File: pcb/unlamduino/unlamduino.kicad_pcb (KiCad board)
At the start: 2 copper layers, 106.7 x 69.8 mm, 41 parts, among them IC2 ATMEGA328-P, P3 CONN_01X08, U1 LM2576, U2 AP111733, Y2 16MHz

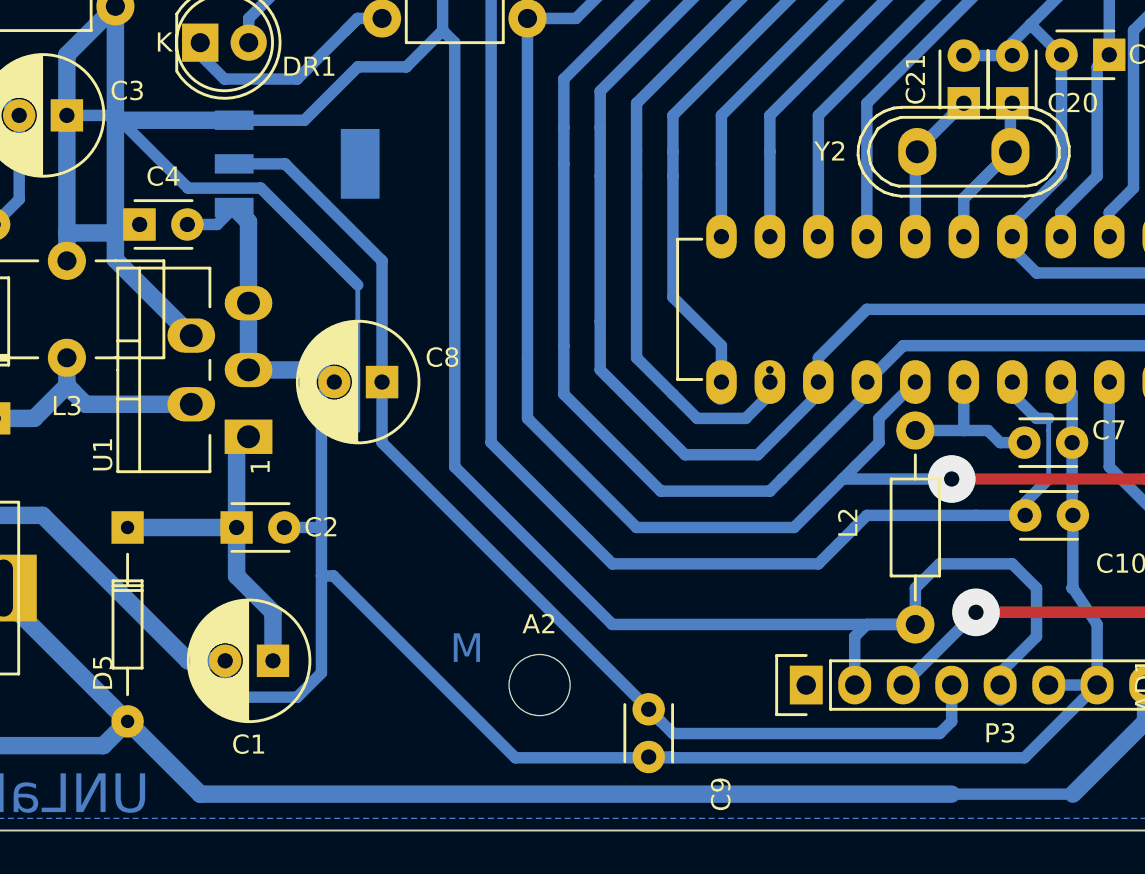
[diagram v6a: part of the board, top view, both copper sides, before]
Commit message: cambio de 5v en conector para no pasar por el medio de un capa.
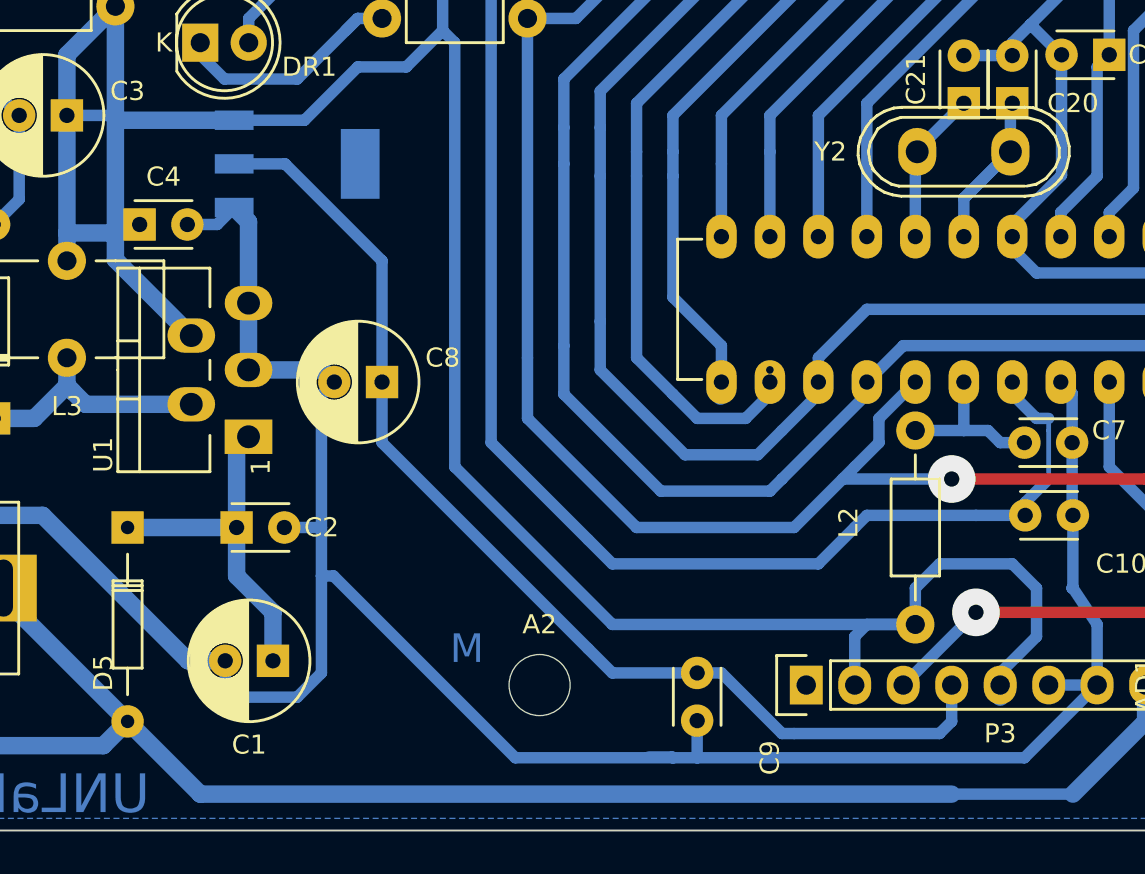
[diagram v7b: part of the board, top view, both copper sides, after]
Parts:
- moved C9 3.17 mm to (199.4, 100.3)
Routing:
- net +5V: track 341.6 -> 317.9 mm
- net GND: track 449.4 -> 451.3 mm
- net +3V3: track 59.2 -> 58.3 mm
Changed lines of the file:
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@@
     (thickness 1.6)
     (drawings 16)
-    (tracks 542)
+    (tracks 543)
     (zones 0)
     (modules 41)
@@
   )
   (module Capacitors_ThroughHole:C_Disc_D3_P2.5 (layer F.Cu)
-    (at 196.85 102.235 270)
+    (at 199.39 100.33 270)
     (descr "Capacitor 3mm Disc, Pitch 2.5mm")
     (tags Capacitor)
@@
   (segment (start 199.39 49.53) (end 226.695 49.53) (width 0.6) (layer B.Cu) (net 6))
   (segment (start 198.501 52.705) (end 198.501 51.689) (width 0.9144) (layer B.Cu) (net 6) (status 30))
-  (segment (start 196.85 104.735) (end 198.08 104.735) (width 0.6) (layer B.Cu) (net 7) (status 400000))
+  (segment (start 199.39 104.775) (end 199.39 102.83) (width 0.6) (layer B.Cu) (net 7) (status 800000))
+  (segment (start 196.85 104.735) (end 198.08 104.735) (width 0.6) (layer B.Cu) (net 7))
   (segment (start 198.08 104.735) (end 198.12 104.775) (width 0.6) (layer B.Cu) (net 7))
   (segment (start 180.3 59.055) (end 180.34 59.055) (width 0.6) (layer B.Cu) (net 7))
@@
   (segment (start 177.8 64.135) (end 179.07 62.865) (width 0.6) (layer B.Cu) (net 7))
   (segment (start 189.865 104.775) (end 198.12 104.775) (width 0.6) (layer B.Cu) (net 7))
-  (segment (start 198.12 104.775) (end 216.535 104.775) (width 0.6) (layer B.Cu) (net 7))
+  (segment (start 198.12 104.775) (end 199.39 104.775) (width 0.6) (layer B.Cu) (net 7))
+  (segment (start 199.39 104.775) (end 216.535 104.775) (width 0.6) (layer B.Cu) (net 7))
   (segment (start 189.865 104.775) (end 180.34 95.25) (width 0.6) (layer B.Cu) (net 7))
   (segment (start 179.705 95.25) (end 180.34 95.25) (width 0.6) (layer B.Cu) (net 7))
@@
   (segment (start 175.26 88.57996) (end 175.88484 87.95512) (width 0.6) (layer B.Cu) (net 8) (status 30))
   (segment (start 169.54754 92.71052) (end 174.93944 92.71052) (width 0.9144) (layer B.Cu) (net 8) (status 30))
-  (segment (start 210.82 97.79) (end 194.945 97.79) (width 0.6) (layer B.Cu) (net 9) (status 400000))
+  (segment (start 210.82 97.79) (end 194.945 97.79) (width 0.6) (layer B.Cu) (net 9))
   (segment (start 186.69 67.31) (end 186.055 66.675) (width 0.6) (layer B.Cu) (net 9))
   (segment (start 186.69 89.535) (end 186.69 67.31) (width 0.6) (layer B.Cu) (net 9))
   (segment (start 194.945 97.79) (end 186.69 89.535) (width 0.6) (layer B.Cu) (net 9))
-  (segment (start 215.265 100.965) (end 215.265 100.33) (width 0.6) (layer B.Cu) (net 9) (status C00000))
-  (segment (start 215.265 100.33) (end 217.17 98.425) (width 0.6) (layer B.Cu) (net 9) (status 400000))
-  (segment (start 210.82 95.885) (end 210.82 97.79) (width 0.6) (layer B.Cu) (net 9) (status 800000))
+  (segment (start 215.265 100.965) (end 215.265 100.33) (width 0.6) (layer B.Cu) (net 9))
+  (segment (start 215.265 100.33) (end 217.17 98.425) (width 0.6) (layer B.Cu) (net 9))
+  (segment (start 210.82 95.885) (end 210.82 97.79) (width 0.6) (layer B.Cu) (net 9))
   (segment (start 212.09 94.615) (end 210.82 95.885) (width 0.6) (layer B.Cu) (net 9))
   (segment (start 215.9 94.615) (end 212.09 94.615) (width 0.6) (layer B.Cu) (net 9))
@@
   (segment (start 224.79 60.96) (end 222.25 63.5) (width 0.9144) (layer B.Cu) (net 9))
   (segment (start 166.37 78.74) (end 166.37 77.2795) (width 0.9144) (layer B.Cu) (net 9))
-  (segment (start 181.61 87.63) (end 181.61 80.01) (width 0.25) (layer B.Cu) (net 9))
-  (segment (start 181.61 80.01) (end 176.53 74.93) (width 0.6) (layer B.Cu) (net 9))
-  (segment (start 172.72 74.93) (end 169.164 71.374) (width 0.6) (layer B.Cu) (net 9))
-  (segment (start 176.53 74.93) (end 172.72 74.93) (width 0.6) (layer B.Cu) (net 9))
   (segment (start 166.37 77.2795) (end 169.7355 77.2795) (width 0.6) (layer B.Cu) (net 9) (status 30))
   (segment (start 169.7355 77.2795) (end 170.18 76.835) (width 0.6) (layer B.Cu) (net 9) (status 30))
@@
   (segment (start 213.36 87.63) (end 210.82 87.63) (width 0.6) (layer B.Cu) (net 11))
   (segment (start 213.36 85.09) (end 213.36 85.725) (width 0.6) (layer B.Cu) (net 11) (status 30))
-  (segment (start 196.85 102.235) (end 197.485 102.87) (width 0.6) (layer B.Cu) (net 12) (status 400000))
+  (segment (start 204.47 103.505) (end 203.835 103.505) (width 0.6) (layer B.Cu) (net 12))
+  (segment (start 200.66 100.33) (end 199.39 100.33) (width 0.6) (layer B.Cu) (net 12) (status 800000))
+  (segment (start 203.835 103.505) (end 200.66 100.33) (width 0.6) (layer B.Cu) (net 12))
+  (segment (start 199.39 100.33) (end 194.945 100.33) (width 0.6) (layer B.Cu) (net 12) (status 400000))
+  (segment (start 194.945 100.33) (end 193.675 99.06) (width 0.6) (layer B.Cu) (net 12))
   (segment (start 182.88 85.09) (end 182.88 88.265) (width 0.6) (layer B.Cu) (net 12))
   (segment (start 212.725 102.87) (end 212.725 100.965) (width 0.6) (layer B.Cu) (net 12))
   (segment (start 212.09 103.505) (end 212.725 102.87) (width 0.6) (layer B.Cu) (net 12))
-  (segment (start 198.12 103.505) (end 212.09 103.505) (width 0.6) (layer B.Cu) (net 12))
-  (segment (start 182.88 88.265) (end 197.485 102.87) (width 0.6) (layer B.Cu) (net 12))
-  (segment (start 197.485 102.87) (end 198.12 103.505) (width 0.6) (layer B.Cu) (net 12))
+  (segment (start 204.47 103.505) (end 212.09 103.505) (width 0.6) (layer B.Cu) (net 12))
+  (segment (start 182.88 88.265) (end 193.675 99.06) (width 0.6) (layer B.Cu) (net 12))
   (segment (start 182.88 85.725) (end 182.88 85.09) (width 0.6) (layer B.Cu) (net 12))
   (segment (start 182.88 85.09) (end 182.88 78.74) (width 0.6) (layer B.Cu) (net 12))

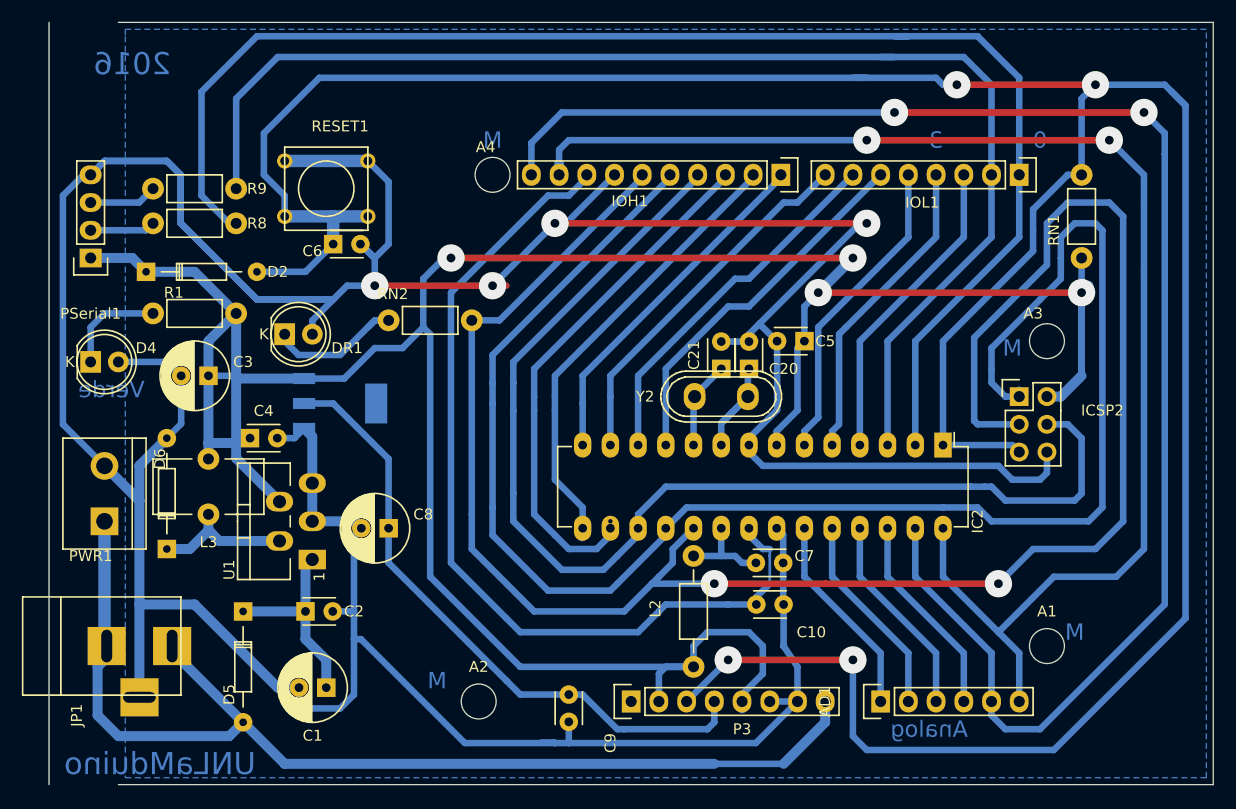
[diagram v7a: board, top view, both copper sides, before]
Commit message: Ajuste de la fuente a la nueva distribución de pistas para planchar.
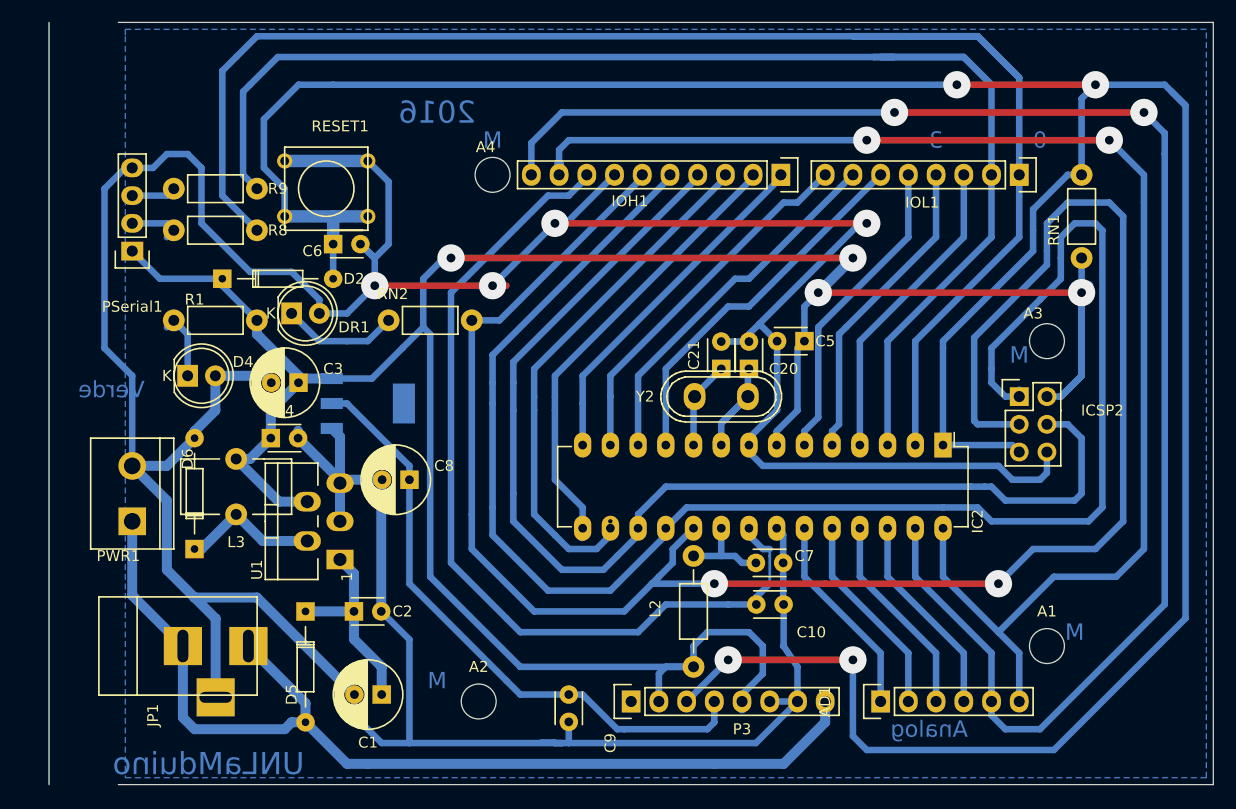
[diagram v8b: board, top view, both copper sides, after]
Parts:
- moved D4 8.98 mm to (164.5, 71.1)
- moved C3 8.28 mm to (174.6, 71.8)
- moved D2 7.01 mm to (167.6, 62.2)
- moved JP1 6.99 mm to (163.8, 95.9)
- moved D5 5.72 mm to (175.3, 92.7)
- moved C1 5.12 mm to (182.2, 100.3)
- moved C8 4.84 mm to (184.8, 80.6)
- moved C2 4.45 mm to (179.7, 92.7)
- moved PSerial1 3.86 mm to (159.4, 59.7)
- moved L3 2.54 mm to (163.8, 83.8)
- moved D6 2.54 mm to (165.1, 87.0)
- moved PWR1 2.54 mm to (159.4, 81.9)
- moved U1 2.54 mm to (174.6, 84.5)
- moved U2 2.54 mm to (181.0, 73.7)
- moved DR1 2.01 mm to (174.0, 65.4)
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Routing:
- net +5V: track 317.9 -> 245.4 mm
- net GND: track 451.3 -> 391.1 mm
- net /IO0: track 131.2 -> 148.2 mm
- net /IO1: track 118.3 -> 130.4 mm
- net /RESET: track 271.5 -> 265.6 mm
- net Net-(D6-Pad1): track 17.2 -> 12.7 mm
- net Net-(D4-Pad1): track 9.42 -> 6.50 mm
- net Net-(PSerial1-Pad3): track 6.24 -> 4.07 mm
- net +3V3: track 58.3 -> 56.7 mm
- net Net-(DR1-Pad1): track 12.9 -> 11.4 mm
- net Net-(PSerial1-Pad2): track 5.98 -> 4.97 mm
- net Net-(C1-Pad1): track 19.1 -> 18.1 mm
- net /VIN: track 109.5 -> 108.6 mm
